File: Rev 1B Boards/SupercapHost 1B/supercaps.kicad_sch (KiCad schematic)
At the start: 21 parts, among them J1 XT30_F, J2 XT30_F, Q1 2SCR587D3, Q2 2SAR587D3, U1 TLV9301xDBV

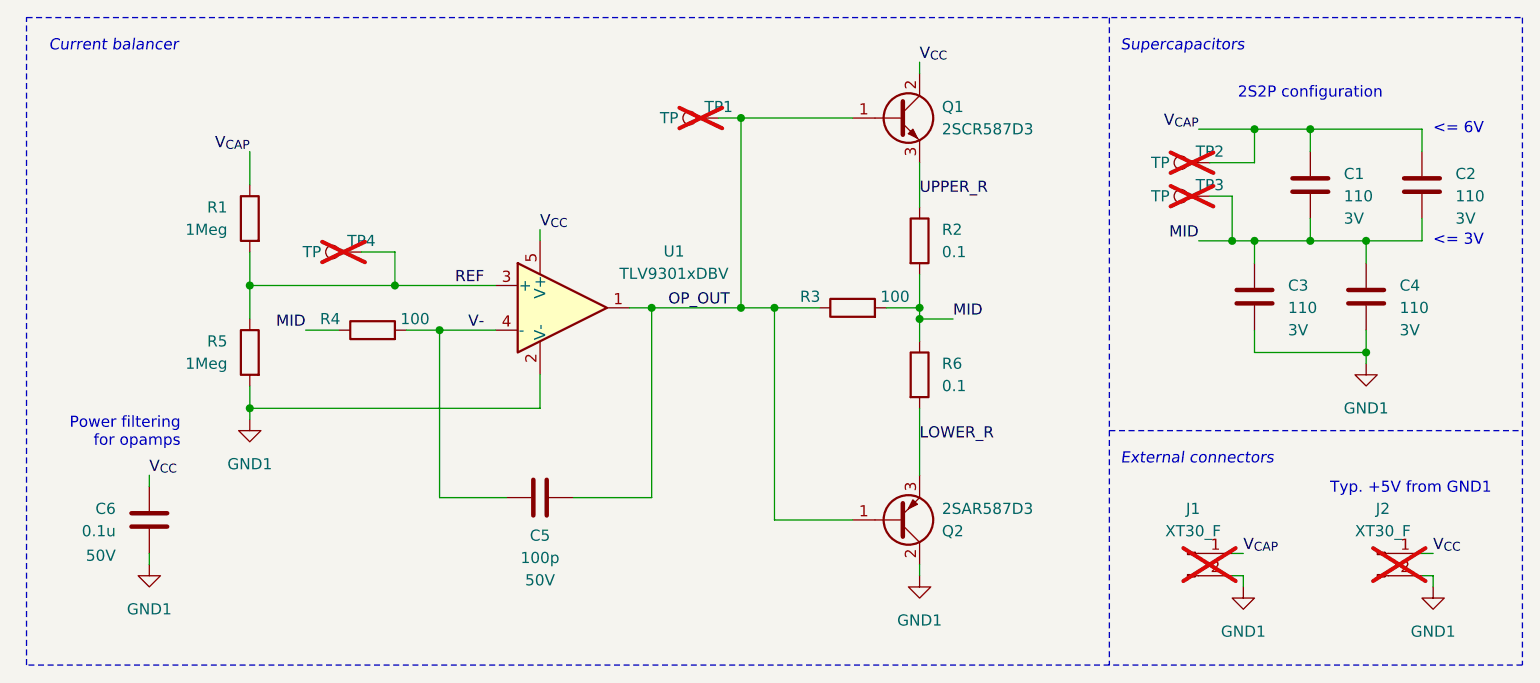
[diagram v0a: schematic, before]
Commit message: Completed layout of supercap host board
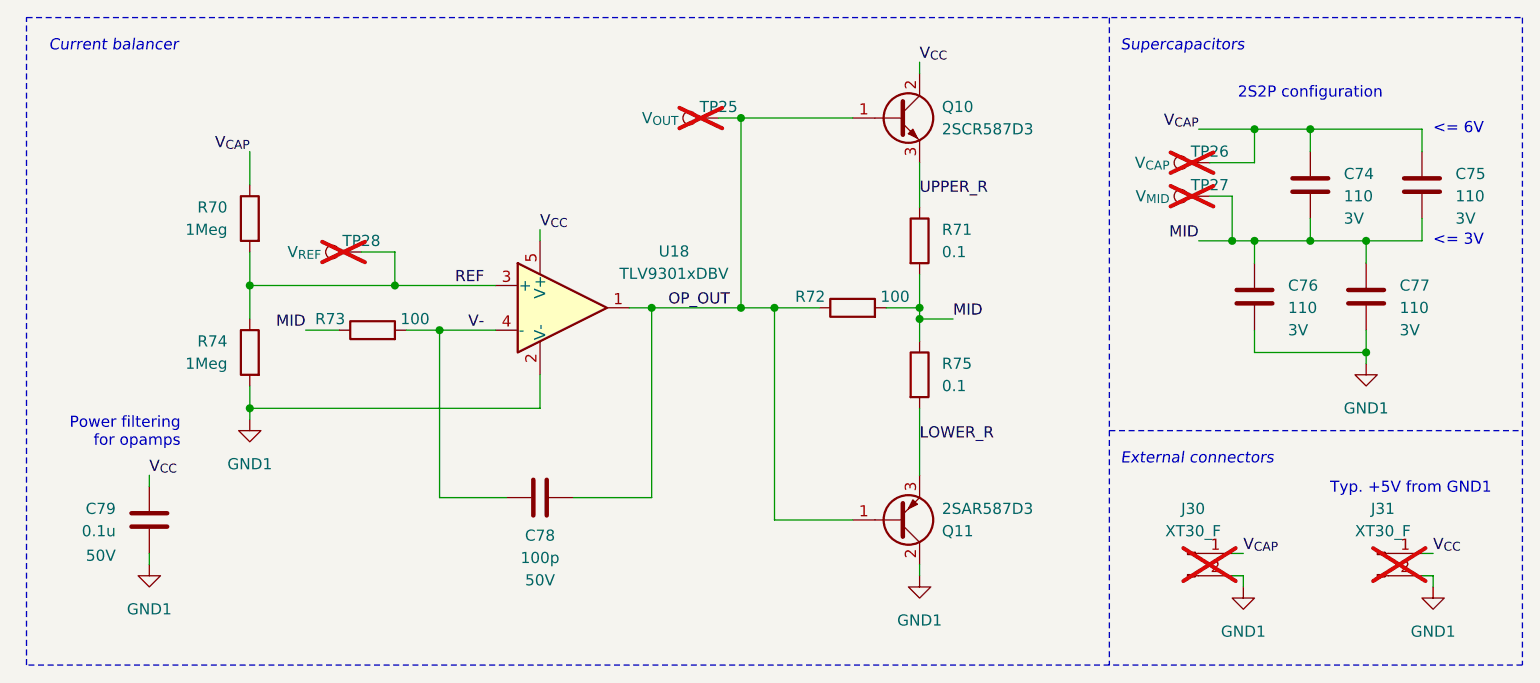
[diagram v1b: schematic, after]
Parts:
- TP25: renamed from TP1; value TP -> V_{OUT}; footprint TestPoint:TestPoint_Pad_1.0x1.0mm -> TestPoint:TestPoint_Bridge_Pitch2.0mm_Drill0.7mm
- TP26: renamed from TP2; value TP -> V_{CAP}
- TP27: renamed from TP3; value TP -> V_{MID}
- TP28: renamed from TP4; value TP -> V_{REF}; footprint TestPoint:TestPoint_Pad_1.0x1.0mm -> TestPoint:TestPoint_Bridge_Pitch2.0mm_Drill0.7mm
- renumbered C1 to C74, C2 to C75, C3 to C76, C4 to C77, C5 to C78, C6 to C79, J1 to J30, J2 to J31, Q1 to Q10, Q2 to Q11, R1 to R70, R2 to R71, R3 to R72, R4 to R73, R5 to R74, R6 to R75, U1 to U18
